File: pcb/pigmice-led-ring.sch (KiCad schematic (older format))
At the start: 27 parts, among them J1 Conn_02x20_Odd_Even, J2 Conn_01x02_Female, U1 TPS61165, U2 LMR33630

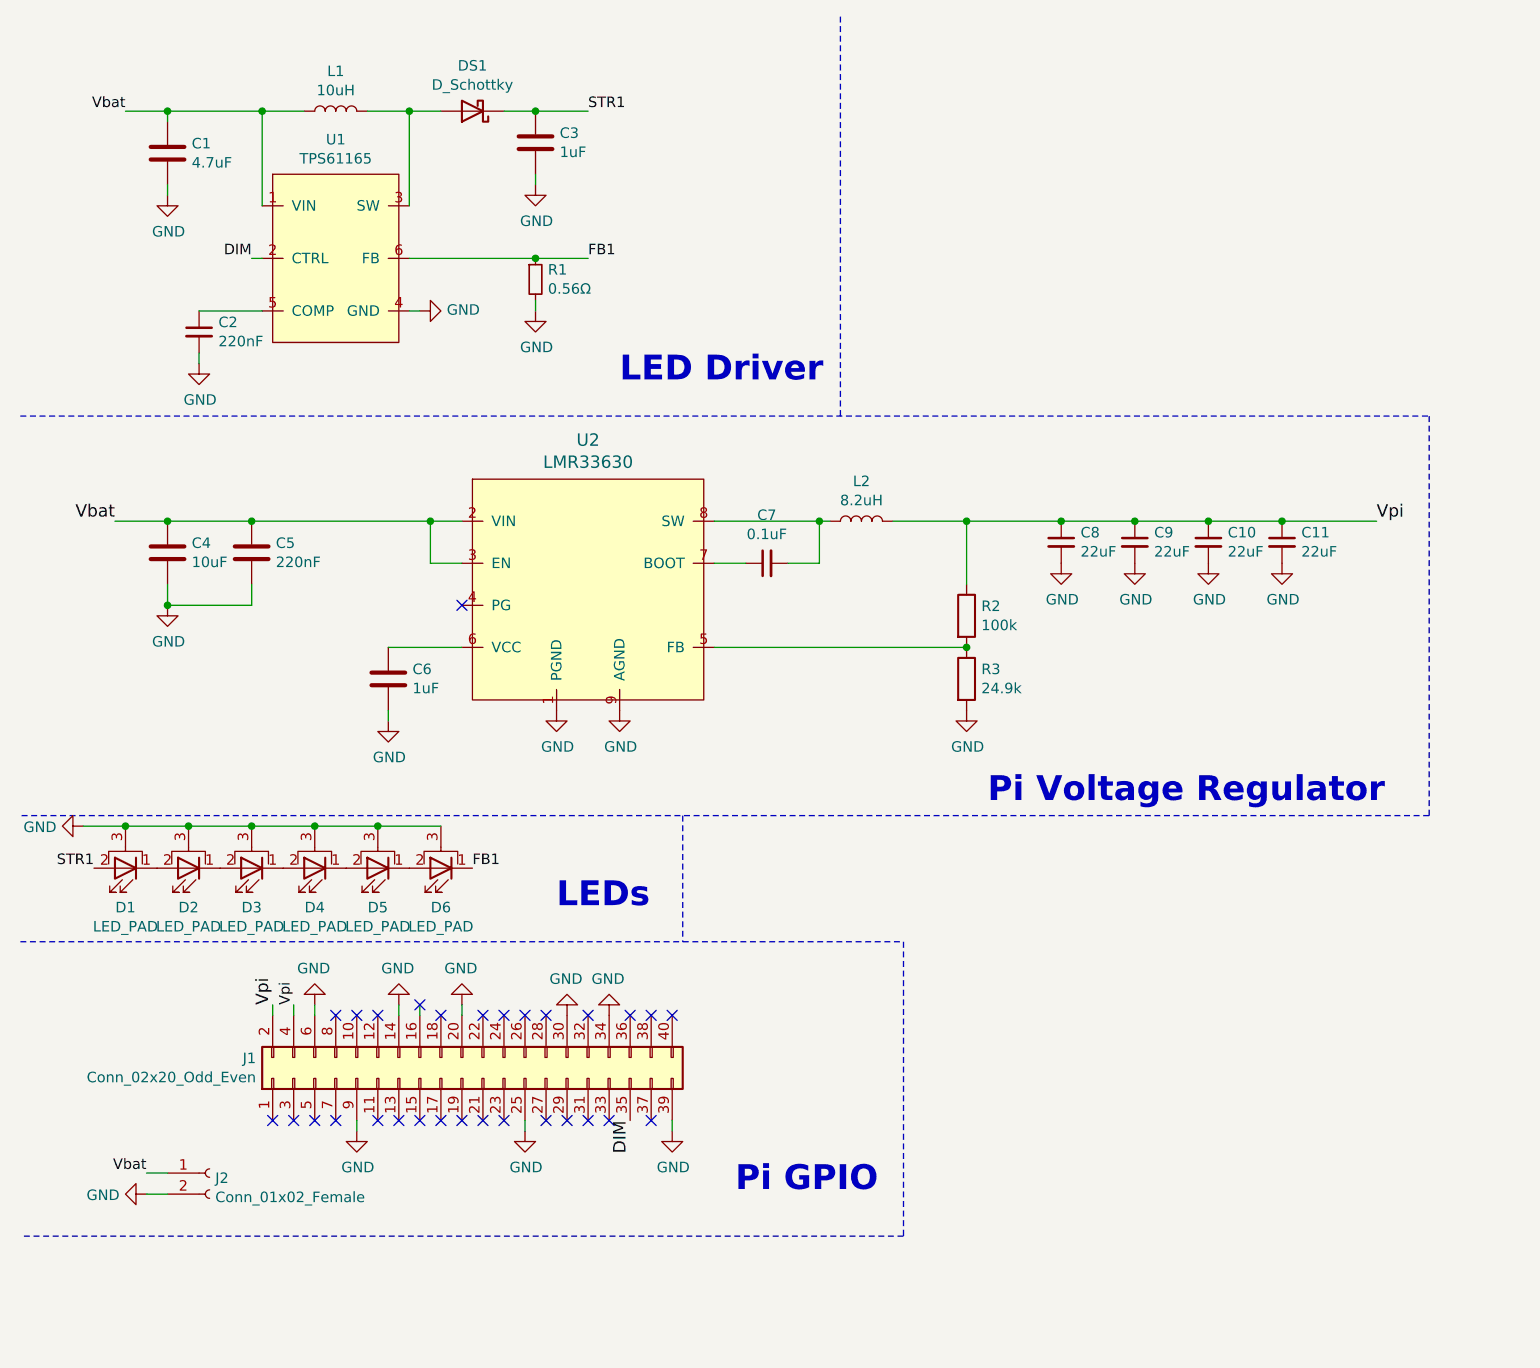
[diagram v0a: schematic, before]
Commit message: Clean up libraries, schematic, PCB
* Consolidate footprint and symbol libraries
* Fix Cree XP E-2 thermal vias
* GND planes on both sides
* Vpi copper fill on both sides, connected with vias
* No Vbat copper fill, replaced with 1mm trace
* Fix all DRC and ERC errors
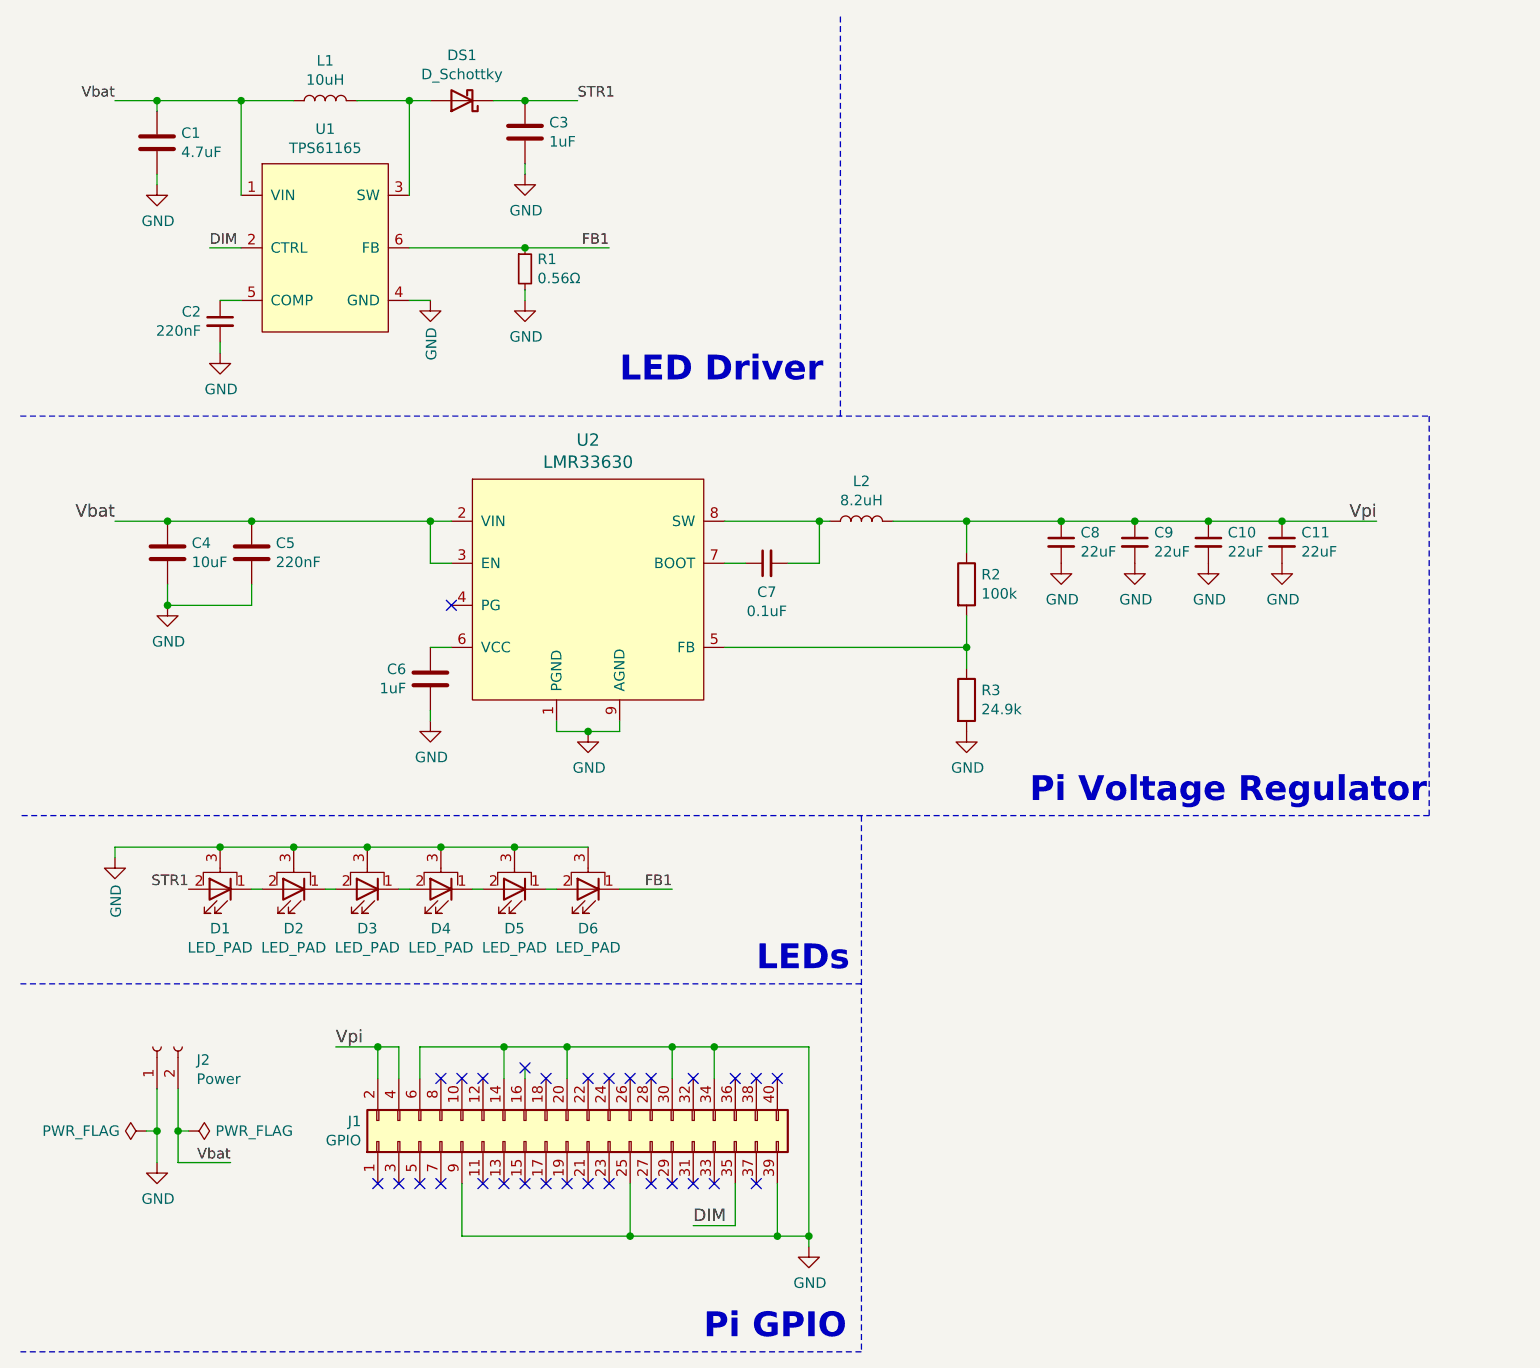
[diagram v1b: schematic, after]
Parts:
- removed U1: TPS61165, Package_TO_SOT_SMD:SOT-23-6, symbol TPS61165:TPS61165
- removed U2: LMR33630, Package_SO:Texas_HSOP-8-1EP_3.9x4.9mm_P1.27mm_ThermalVias, symbol LMR33630:LMR33630
- added U1: TPS61165, Package_TO_SOT_SMD:SOT-23-6, symbol pigmice-led-ring:TPS61165
- added U2: LMR33630, Package_SO:Texas_HSOP-8-1EP_3.9x4.9mm_P1.27mm_ThermalVias, symbol pigmice-led-ring:LMR33630
- D1, D2, D3, D4, D5, D6: footprint LED_SMD:LED_Cree-XP -> pigmice-led-ring:LED_Cree-XP
- J1: value Conn_02x20_Odd_Even -> GPIO
- J2: value Conn_01x02_Female -> Power; footprint led-ring:TE_282837-2 -> pigmice-led-ring:TE_282837-2
- L1: footprint led-ring:IND_#A915AY-100M=P3 -> pigmice-led-ring:IND_#A915AY-100M=P3
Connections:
- net DIM: now also U1.2 (CTRL)
- net FB1: now also U1.6 (FB)
- net GND: now also J2.1 (Pin_1), U1.4 (GND), U2.1 (PGND), U2.9 (AGND); no longer J2.2 (Pin_2)
- net Vbat: now also J2.2 (Pin_2), U1.1 (VIN), U2.2 (VIN), U2.3 (EN); no longer J2.1 (Pin_1)
- net at DS1.2 (A), L1.2: now also U1.3 (SW)
- net at C2.1: now also U1.5 (COMP)
- net at R2.2, R3.1: now also U2.5 (FB)
- net at C6.1: now also U2.6 (VCC)
- net at C7.1: now also U2.7 (BOOT)
- net at C7.2, L2.1: now also U2.8 (SW)
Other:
- moved on the sheet: C1, C2, C3, C6, D1, DS1, J1, J2, L1, R1, R2, R3

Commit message: Add DIM pull-down, fixup BOM, zone tolerances
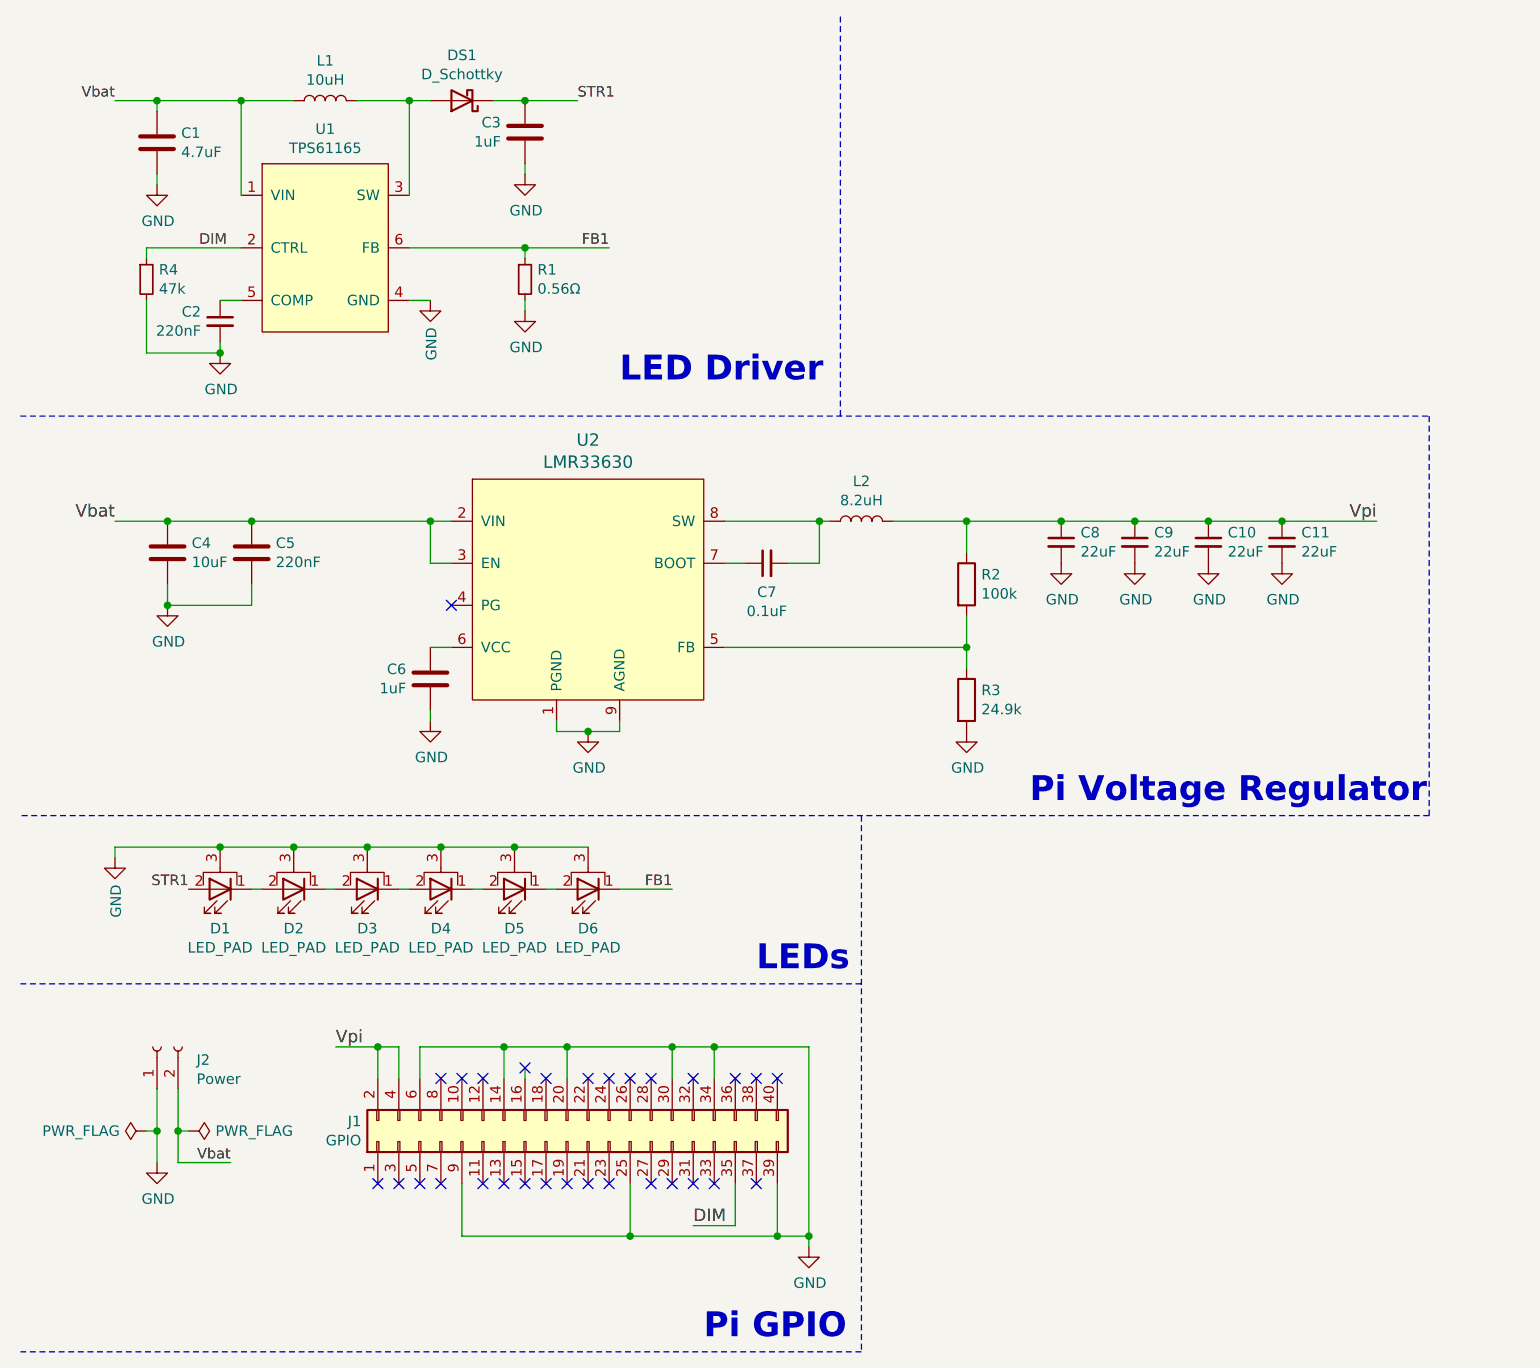
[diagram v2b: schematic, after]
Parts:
- added R4: 47k, Resistor_SMD:R_0805_2012Metric, symbol Device:R_Small
- C1: Digikey (none) -> 445-172480-1-ND; P/N (none) -> CGA4J1X7R1V475M125AE
- C10, C11, C8, C9: Digikey (none) -> 490-14682-1-ND; P/N (none) -> GRM32ER71E226ME15K
- C2: Digikey (none) -> 490-13311-1-ND; P/N (none) -> GCM21BR71H224KA37K
- C3: footprint Capacitor_SMD:C_0805_2012Metric -> Capacitor_SMD:C_0603_1608Metric; Digikey (none) -> 1276-6524-1-ND; P/N (none) -> CL10B105MO8NNWC
- C4: Digikey (none) -> 1276-3388-1-ND; P/N (none) -> CL32B106KBJNNWE
- C5: Digikey (none) -> 490-5402-1-ND; P/N (none) -> GCM188R71H224KA64D
- C6: Digikey (none) -> 1276-6524-1-ND; P/N (none) -> CL10B105MO8NNWC
- C7: Digikey (none) -> 490-16327-1-ND; P/N (none) -> GRM188R72A104MA35D
- D1, D2, D3, D4, D5, D6: Digikey (none) -> XPEBGR-L1-0000-00D01CT-ND; P/N (none) -> XPEBGR-L1-0000-00D01
- DS1: Digikey (none) -> MBR0540CT-ND; P/N (none) -> MBR0540
- J1: Digikey (none) -> A26468-ND; P/N (none) -> 2-534206-0
- J2: Digikey (none) -> A113320-ND; P/N (none) -> 282837-2
- L1: Digikey (none) -> 490-16513-1-ND; P/N (none) -> #A915AY-100M=P3
- L2: Digikey (none) -> 541-1012-1-ND; P/N (none) -> IHLP2525CZER8R2M01
- R1: Digikey (none) -> P19302CT-ND; P/N (none) -> ERJ-6DQFR56V
- R2: Digikey (none) -> P100KDBCT-ND; P/N (none) -> ERA-3AEB104V
- R3: Digikey (none) -> P24.9KDBCT-ND; P/N (none) -> ERA-3AEB2492V
- U1: Digikey (none) -> 296-27597-1-ND; P/N (none) -> TPS61165DBVR
- U2: Digikey (none) -> 296-49763-1-ND; P/N (none) -> LMR33630ADDAR
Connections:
- net DIM: now also R4.1
- net GND: now also R4.2
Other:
- moved on the sheet: R1
